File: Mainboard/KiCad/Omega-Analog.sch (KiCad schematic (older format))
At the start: 95 parts, among them J3 Audio, J6 Cassette, Q1 PN2907A, U48 OPA340P, U49 LM311

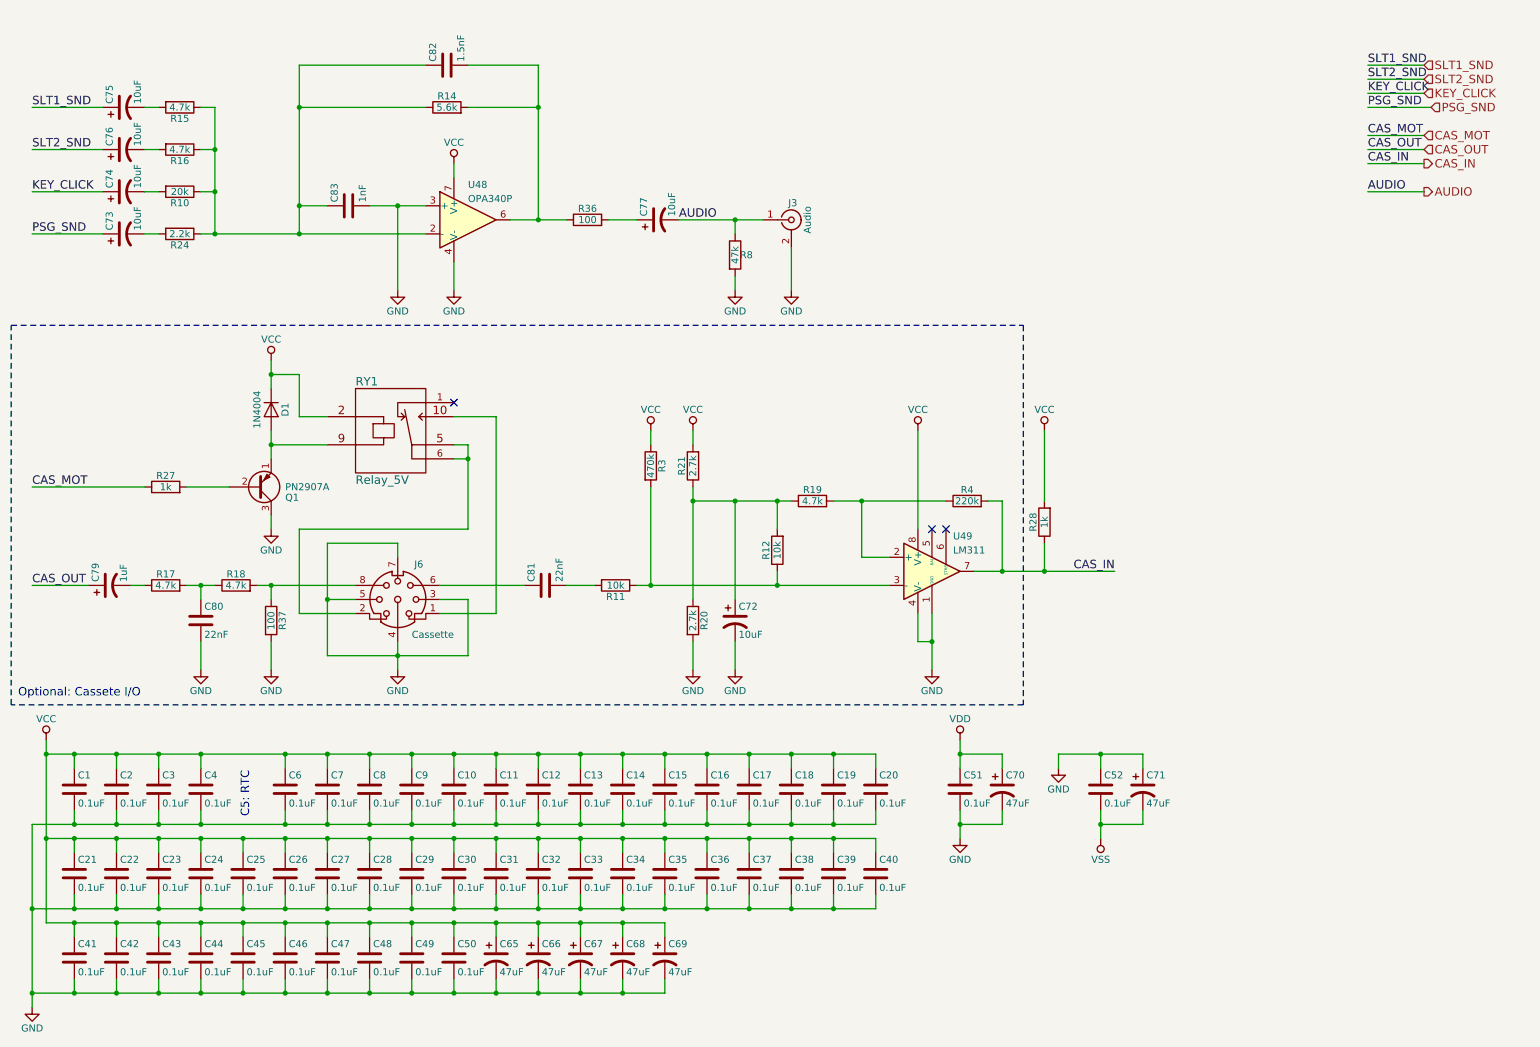
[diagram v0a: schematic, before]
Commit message: Mainboard: Fixed schematic and PCB for v1.1
Signed-off-by: Sergey Kiselev <skiselev@gmail.com>
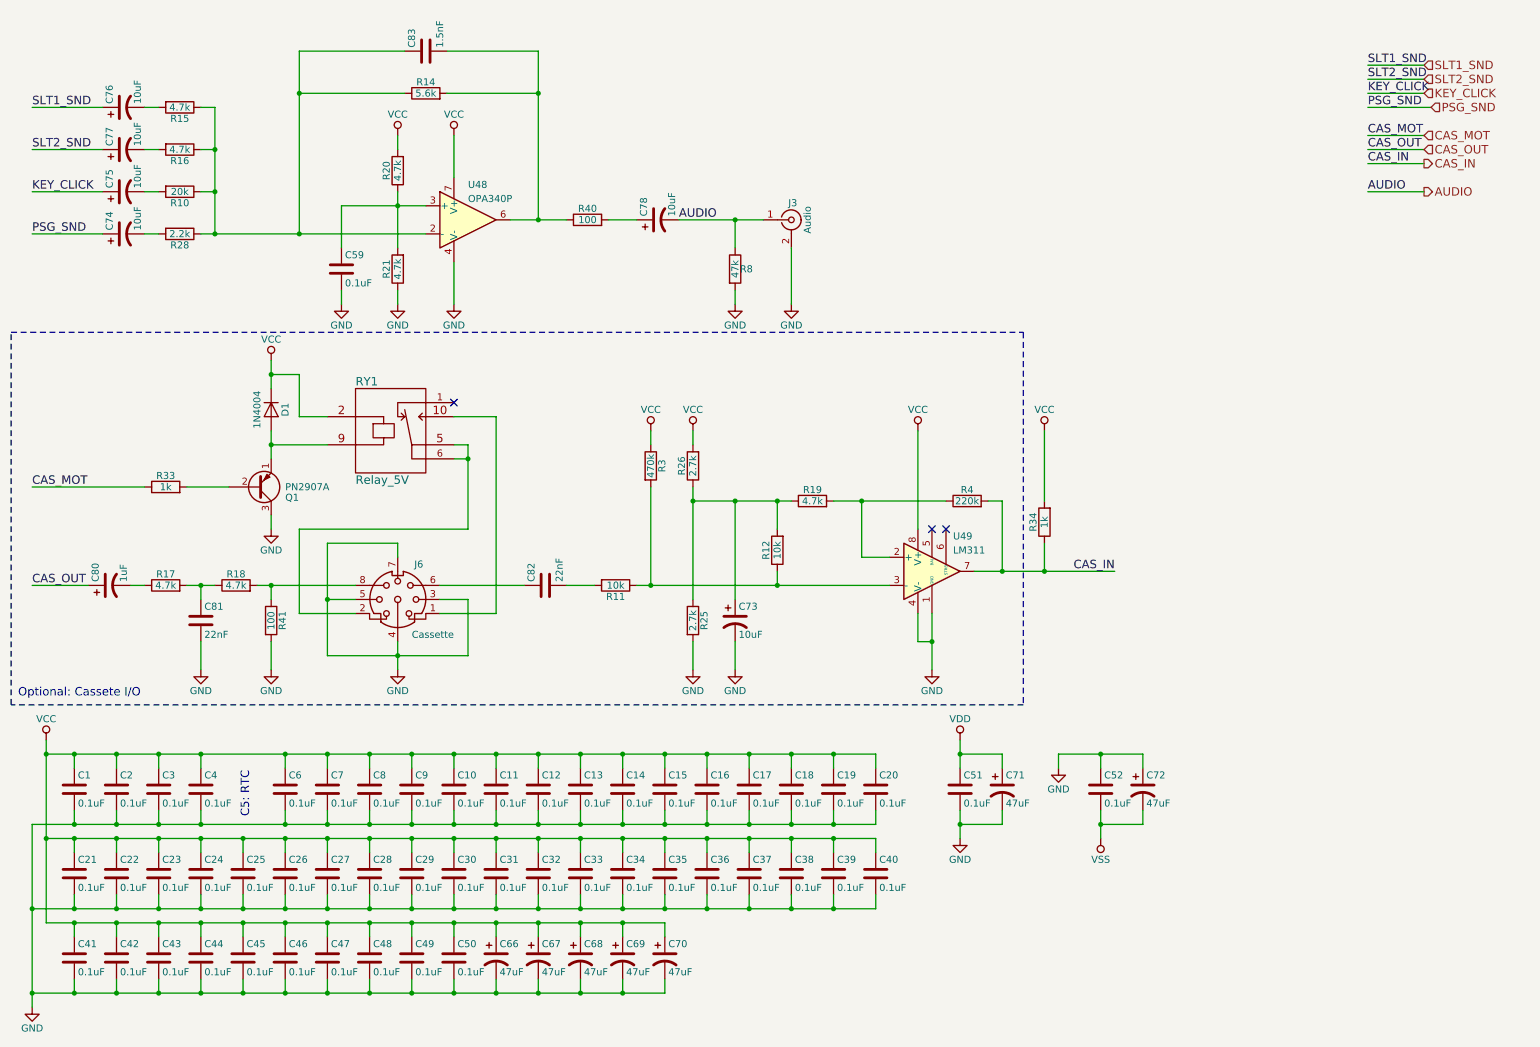
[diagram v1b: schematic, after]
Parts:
- added R20, R21: 4.7k, My_Components:Res_762, symbol Device:R
- C59: renamed from C83; value 1nF -> 0.1uF
- renumbered C65 to C66, C66 to C67, C67 to C68, C68 to C69, C69 to C70, C70 to C71, C71 to C72, C72 to C73, C73 to C74, C74 to C75, C75 to C76, C76 to C77, C77 to C78, C79 to C80, C80 to C81, C81 to C82, C82 to C83, R20 to R25, R21 to R26, R24 to R28, R27 to R33, R28 to R34, R36 to R40, R37 to R41
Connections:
- net GND: now also R21.1; no longer U48.3 (+)
- net VCC: now also R20.2
- net at C83.1, R10.1, R14.1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: no longer C59.1
- new net: C59.1, R20.1, R21.2, U48.3 (+)
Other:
- moved on the sheet: C59, C83, R14, R8

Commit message: Mainboard: Update schematic and PCB layout with latest fixes
Signed-off-by: Sergey Kiselev <skiselev@gmail.com>
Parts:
- removed U48: OPA340P, My_Components:IC_DIP8_300, symbol Amplifier_Operational:OPA340P
- added U48: MCP601, My_Components:IC_DIP8_300, symbol Amplifier_Operational:MCP601-xP
- D1: value 1N4004 -> 1N4148
- U49: symbol Comparator:LM311 -> my_components:LM311
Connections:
- net GND: now also U48.4 (V-)
- net VCC: now also U48.7 (V+)
- net at C83.1, R10.1, R14.1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: now also U48.2 (-)
- net at C83.2, R14.2, R40.1: now also U48.6
- net at C59.1, R20.1, R21.2: now also U48.3 (+)
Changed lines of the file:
@@
 CAS_IN
 $Comp
-L Comparator:LM311 U49
+L my_components:LM311 U49
 U 1 1 5BFD2D8A
 P 7100 4400
@@
 P 2400 3250
 F 0 "D1" H 2400 3350 50  0000 C CNN
-F 1 "1N4004" H 2400 3150 50  0000 C CNN
+F 1 "1N4148" H 2400 3150 50  0000 C CNN
 F 2 "My_Components:Diode_762" H 2400 3250 50  0001 C CNN
 F 3 "" H 2400 3250 50  0001 C CNN
@@
 Text Notes 2250 6150 1    60   ~ 0
 C5: RTC
-$Comp
-L Amplifier_Operational:OPA340P U48
-U 1 1 5C06AE96
-P 3800 1900
-F 0 "U48" H 3800 2150 50  0000 L CNN
-F 1 "OPA340P" H 3800 2050 50  0000 L CNN
-F 2 "My_Components:IC_DIP8_300" H 3800 1900 50  0001 L CNN
-F 3 "" H 3950 2050 50  0001 C CNN
-	1    3800 1900
-	1    0    0    -1
-$EndComp
 Connection ~ 2600 2000
 Connection ~ 3300 1800
@@
 	0    -1   -1   0
 $EndComp
+$Comp
+L Amplifier_Operational:MCP601-xP U48
+U 1 1 5DBEEC00
+P 3800 1900
+F 0 "U48" H 3850 2150 50  0000 L CNN
+F 1 "MCP601" H 3850 2050 50  0000 L CNN
+F 2 "My_Components:IC_DIP8_300" H 3700 1700 50  0001 L CNN
+F 3 "http://ww1.microchip.com/downloads/en/DeviceDoc/21314g.pdf" H 3950 2050 50  0001 C CNN
+	1    3800 1900
+	1    0    0    -1
+$EndComp
 $EndSCHEMATC

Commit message: Mainboard: Fix some of the issues described in #1
Signed-off-by: Sergey Kiselev <skiselev@gmail.com>
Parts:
- removed C51, C52: 0.1uF, My_Components:Cap_Cer_508, symbol Device:C
- removed J6: Cassette, My_Components:Conn_Mini_DIN_8pin, symbol Connector:Mini-DIN-8
- added J6: Cassette, My_Components:Conn_DIN_8pin, symbol Connector:DIN-8
- added L2, L3: 5.7uH, My_Components:Res_762, symbol Device:L_Small
- C58: renamed from C70; value 47uF -> 0.1uF; footprint My_Components:Cap_Elec_Radial_6.3mm -> My_Components:Cap_Cer_508; symbol Device:CP1 -> Device:C
- C68: renamed from C67; value 47uF -> 10uF; footprint My_Components:Cap_Elec_Radial_6.3mm -> My_Components:Cap_Elec_Radial_5mm
- C69: value 47uF -> 10uF; footprint My_Components:Cap_Elec_Radial_6.3mm -> My_Components:Cap_Elec_Radial_5mm
- C70: renamed from C68; value 47uF -> 10uF; footprint My_Components:Cap_Elec_Radial_6.3mm -> My_Components:Cap_Elec_Radial_5mm
- renumbered C59 to C57, C66 to C65, C71 to C66, C72 to C67, C73 to C71, C74 to C72, C75 to C73, C76 to C74, C77 to C75, C78 to C76, C80 to C78, C81 to C79, C82 to C80, C83 to C81, R14 to R15, R15 to R16, R16 to R17, R17 to R18, R18 to R19, R19 to R20, R20 to R21, R21 to R22, R25 to R23, R26 to R24, R28 to R26, R33 to R31, R34 to R32, R40 to R41, R41 to R42
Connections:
- net GND: now also J6.1, J6.2, J6.3, J6.8
- net VCC: now also L2.1, L3.1; no longer C3.1, C47.1, C50.1, C58.1, C69.1, C70.1
- net at C80.1: now also J6.5
- net at R19.2, R42.1: now also J6.4
- net at RY1.10: now also J6.7
- net at RY1.5, RY1.6: now also J6.6
- new net VCCRGB: C47.1, C50.1, C69.1, L3.2
- new net VCCVDP: C3.1, C58.1, C70.1, L2.2
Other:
- moved on the sheet: C10, C11, C12, C13, C14, C15, C16, C17, C18, C19, C20, C21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
